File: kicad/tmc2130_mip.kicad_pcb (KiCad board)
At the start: 4 copper layers, 100 x 90 mm, 226 parts, among them J1 Conn_01x06_Pin, J10 Phoenix 1987096, J11 Conn_01x03_Pin, J12 Conn_01x03_Pin, J13 Conn_01x03_Pin, J2 Conn_01x06_Pin, J3 PHOENIX CONTACT 1755752, J4 Conn_Coaxial, J5 PHOENIX CONTACT 1755752, J7 PHOENIX CONTACT 1755752, J9 USB4105-GF-A, M1 32001505/6CEU, Q1 DMPH6050SK3-13, Q2 BS870, Q3 BS870, U2 FT230XQ, U3 USBLC6-2SC6, U4 LMR51610XDBVR, U5 ISM330DLCTR, U6 TXS0102DCUR, U7 AP2127K-ADJTRG1, U8 MCP6001-OT, U9 MCP6001-OT

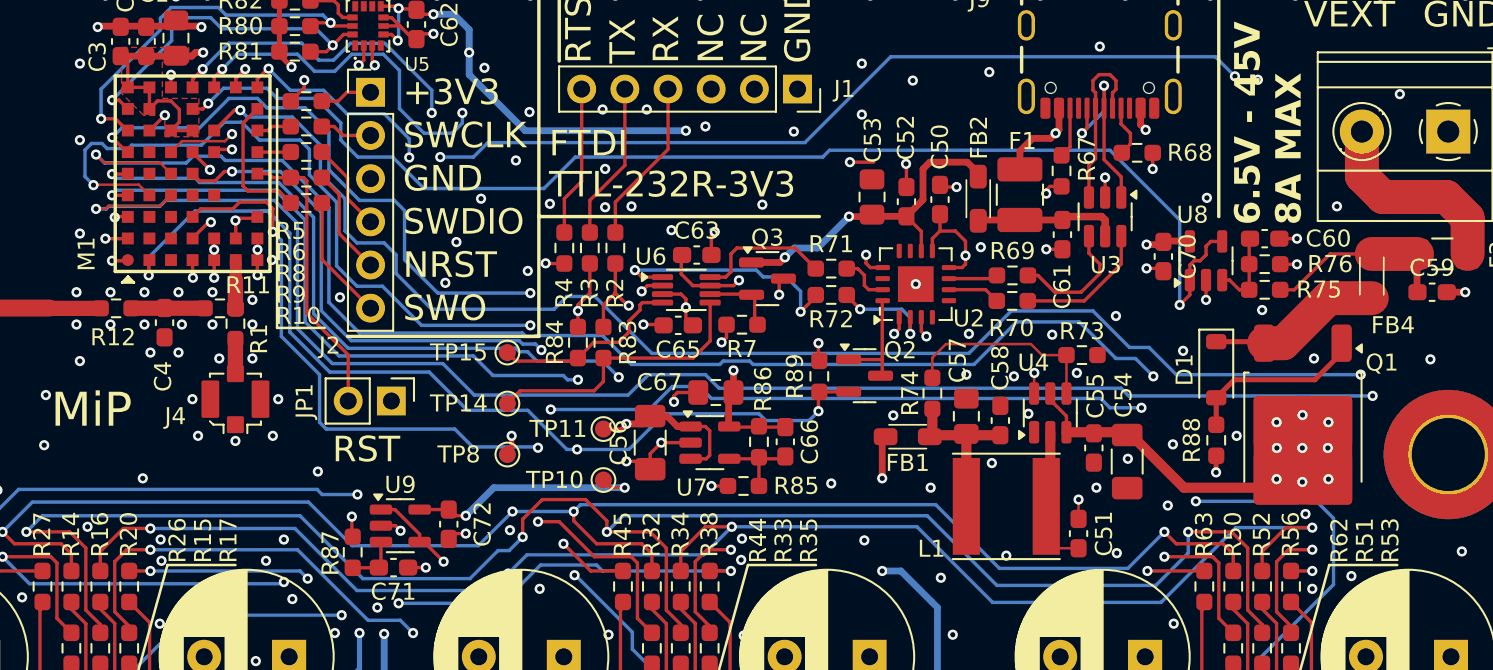
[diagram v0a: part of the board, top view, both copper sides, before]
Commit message: fixed layout error on u4
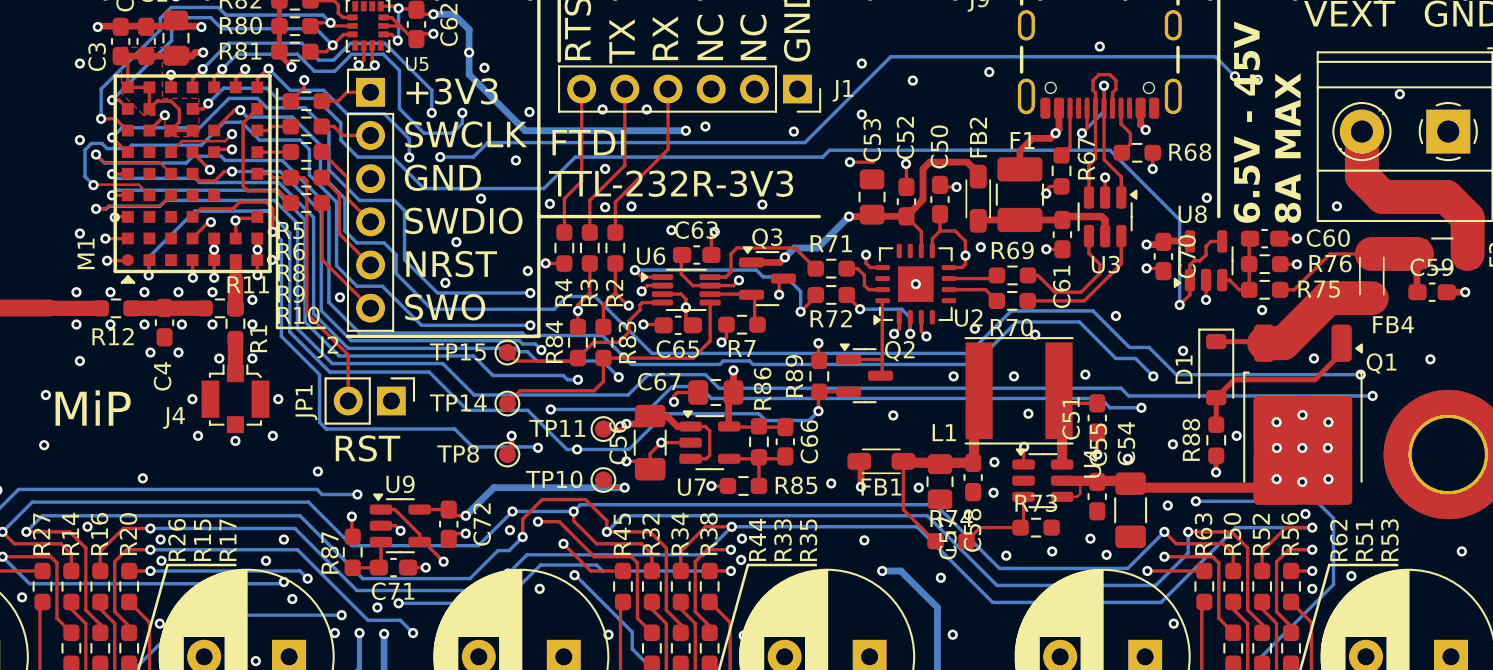
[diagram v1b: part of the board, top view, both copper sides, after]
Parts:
- moved R73 10.5 mm to (159.8, 101.3)
- moved R74 8.77 mm to (154.8, 102.1), turned to 0 degrees
- moved C51 6.89 mm to (163.3, 94.8), turned to 90 degrees
- moved L1 6.84 mm to (158.8, 93.2)
- moved C57 4.15 mm to (154.1, 98.6), turned to 90 degrees
- moved U4 4.01 mm to (160.2, 98.5), turned to 0 degrees
- moved C58 3.71 mm to (156.1, 98.3), turned to -90 degrees
- moved C54 2.87 mm to (165.3, 100.3)
- moved C55 2.87 mm to (163.3, 99.5)
- moved FB1 2.12 mm to (150.7, 97.4)
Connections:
- U4 pad 1: GND -> Net-(U4-CB)
- U4 pad 2: Net-(U4-SW) -> GND
- U4 pad 3: VEXT -> Net-(U4-FB)
- U4 pad 4: Net-(U4-FB) -> VEXT
- U4 pad 6: Net-(U4-CB) -> Net-(U4-SW)
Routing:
- net Net-(U4-FB): track 11.9 -> 5.39 mm
- net Net-(C57-Pad2): track 10.2 -> 15.8 mm
- net Net-(U4-CB): track 10.9 -> 7.32 mm
- net GND: track 167.2 -> 169.0 mm, vias 359 -> 361
- net VEXT: track 314.3 -> 312.6 mm
- net +6V: track 158.9 -> 157.9 mm
- net Net-(U4-SW): track 6.71 -> 7.35 mm
